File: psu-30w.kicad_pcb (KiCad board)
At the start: 2 copper layers, 200 x 81 mm, 42 parts, among them J1 Barrel_Jack, J101 SWITCH, U1 R-78E5.0-1.0

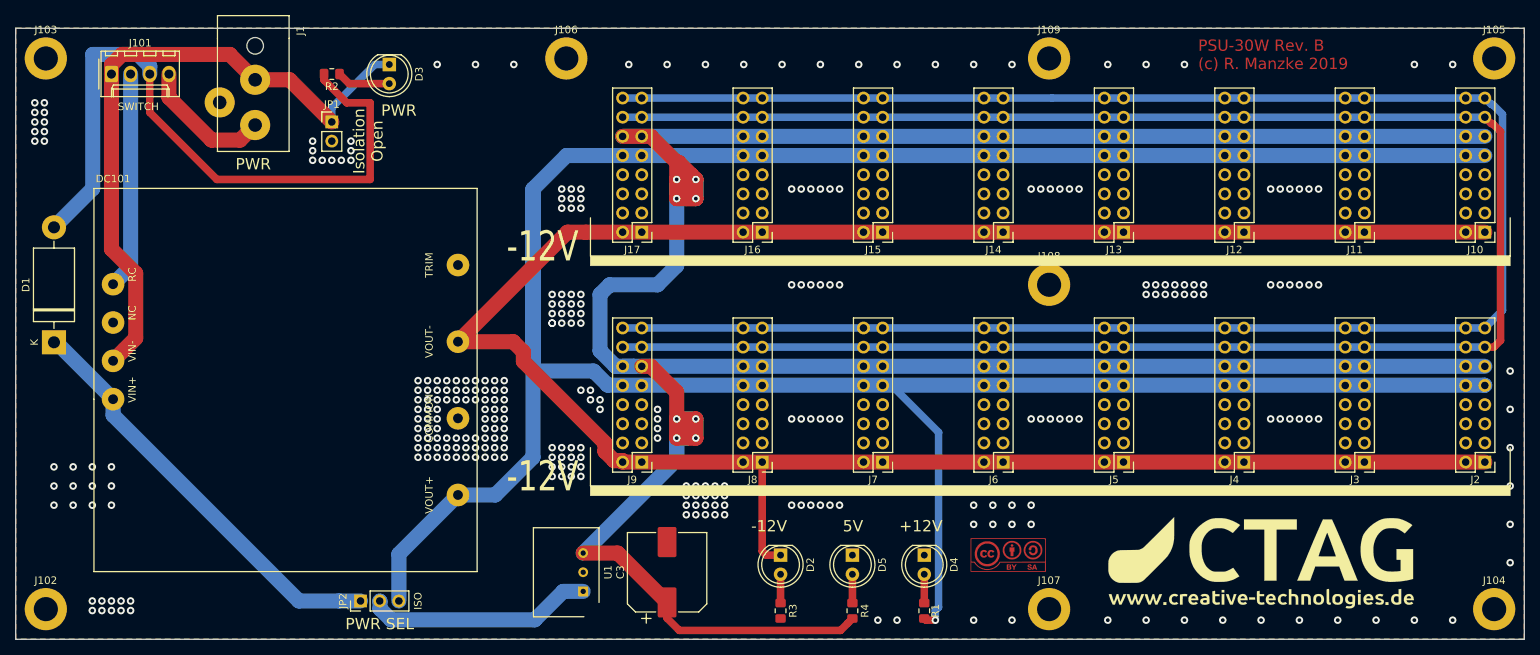
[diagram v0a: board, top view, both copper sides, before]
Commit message: adaptations + simplifications
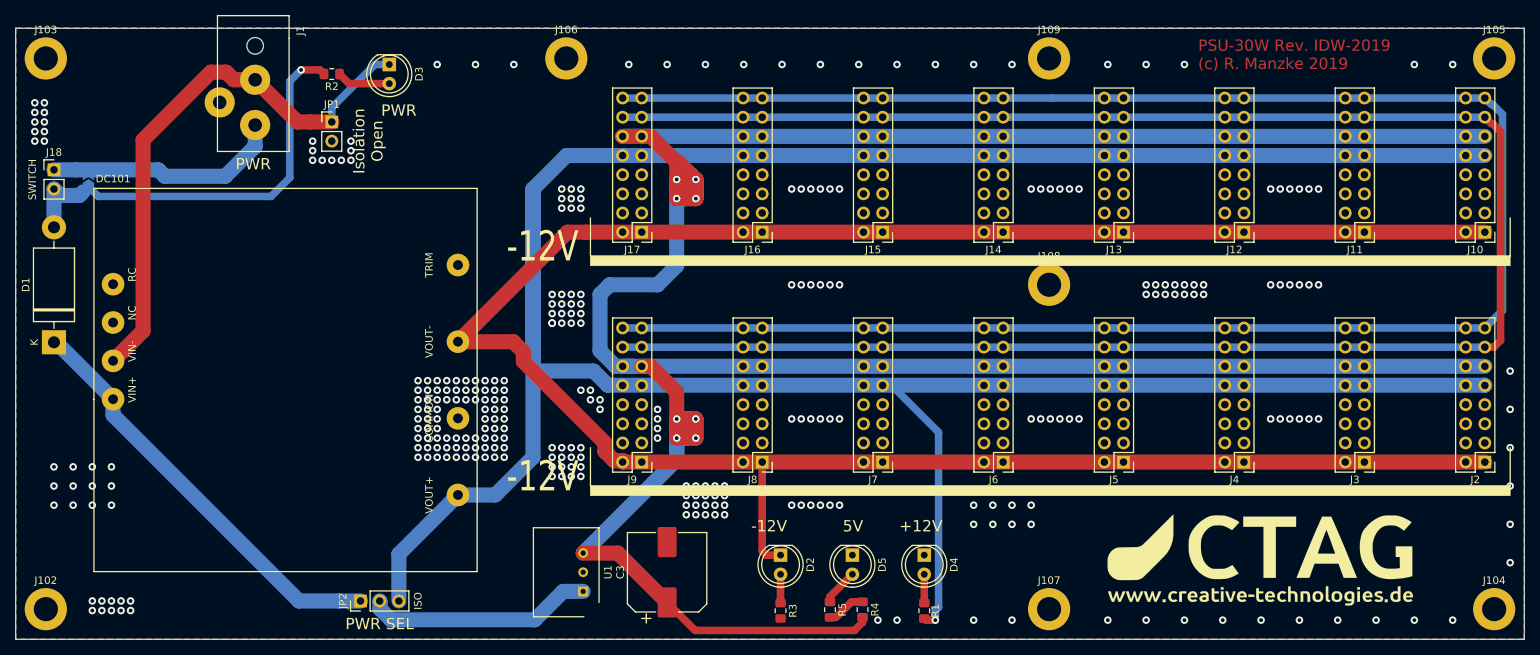
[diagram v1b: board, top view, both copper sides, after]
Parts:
- removed the G*** at (182.6, 118.8)
- removed J101: SWITCH, Connector_Molex:Molex_KK-254_AE-6410-04A_1x04_P2.54mm_Vertical
- added J18: Power Switch Option, Connector_PinHeader_2.54mm:PinHeader_1x02_P2.54mm_Vertical, F.Cu at (56.1, 67.8)
- added JP3: Solder Jumper, Jumper:SolderJumper-2_P1.3mm_Open_TrianglePad1.0x1.5mm, B.Cu at (60.7, 69.3)
- added R5: 4k7, Resistor_SMD:R_0805_2012Metric_Pad1.15x1.40mm_HandSolder, F.Cu at (158.9, 126.1)
- R1, R2, R3: value 560 -> 4k7
- R4: value 180 -> 4k7
- moved R4 1.35 mm to (163.3, 126.1)
- moved G*** 0.38 mm to (216.0, 119.5)
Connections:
- DC101 pad 1: Net-(DC101-Pad1) -> (no net)
- R4 pad 1: Net-(D5-Pad2) -> Net-(R4-Pad1)
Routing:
- net Net-(D1-Pad2): track 90.6 -> 55.9 mm, vias 0 -> 1
- net Net-(DC101-Pad1): track 28.8 -> 0.00 mm
- net Net-(J1-Pad1): track 17.7 -> 31.5 mm
- net Net-(D3-Pad1): track 87.2 -> 74.3 mm
- net Net-(R4-Pad1): track 0.00 -> 5.17 mm
- net Net-(D5-Pad2): track 3.81 -> 4.90 mm
- net +5V: track 411.5 -> 412.0 mm
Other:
- board text added: "PSU-30W Rev. IDW-2019 (c) R. Manzke 2019"
- board text removed: "PSU-30W Rev. B (c) R. Manzke 2019"
